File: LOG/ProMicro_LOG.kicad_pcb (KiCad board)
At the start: 2 copper layers, 17.8 x 30.5 mm, 16 parts, among them J1 Micro_SD_Card_Det, U1 DS3231MZ

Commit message: dump
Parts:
- A1: value Sparkfun_Pro_Micro_3V3 -> Sparkfun_Pro_Micro
- moved LOGO1 10.2 mm to (144.8, 80.0)
- renumbered JP2 to JP1, JP1 to JP2, JP4 to JP3, R6 to R1, R1 to R2, R2 to R3, R5 to R4, R3 to R5, R4 to R6
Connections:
- net Reset renamed ~RST
- A1 pad 10: (no net) -> INT
- A1 pad 11: INT -> (no net)
- A1 pad 3: (no net) -> GND
- A1 pad 7: TRG -> (no net)
- A1 pad 8: (no net) -> PWM
- JP1 pad 2: TRG -> PWM
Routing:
- net PWM: track 0.00 -> 18.7 mm, vias 0 -> 2
- net TRG: track 17.6 -> 0.00 mm, vias 2 -> 0
- net INT: track 12.0 -> 13.1 mm
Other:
- board text added: "3V3"
- board text added: "BTN"
- board text added: "CIPO"
- board text added: "COPI"
- board text added: "CS0"
- board text added: "CS1"
- board text added: "GND"
- board text added: "INT"
- board text added: "PWM"
- board text added: "RST"
- board text added: "SCK"
- board text added: "SCL"
- board text added: "SDA"
- board text added: "VBAT"
- board text added: "nerdyscout.github.io/ ProMicro/LOG v1.2"
- board text removed: "nerdyscout.github.io/ProMicro/LOG"
- board text removed: "v1.1"

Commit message: clean
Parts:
- moved R5 1.91 mm to (140.5, 95.9)
- moved R6 1.91 mm to (140.3, 97.8)
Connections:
- R5 pad 2: SDA -> SCL
- R6 pad 2: SCL -> SDA

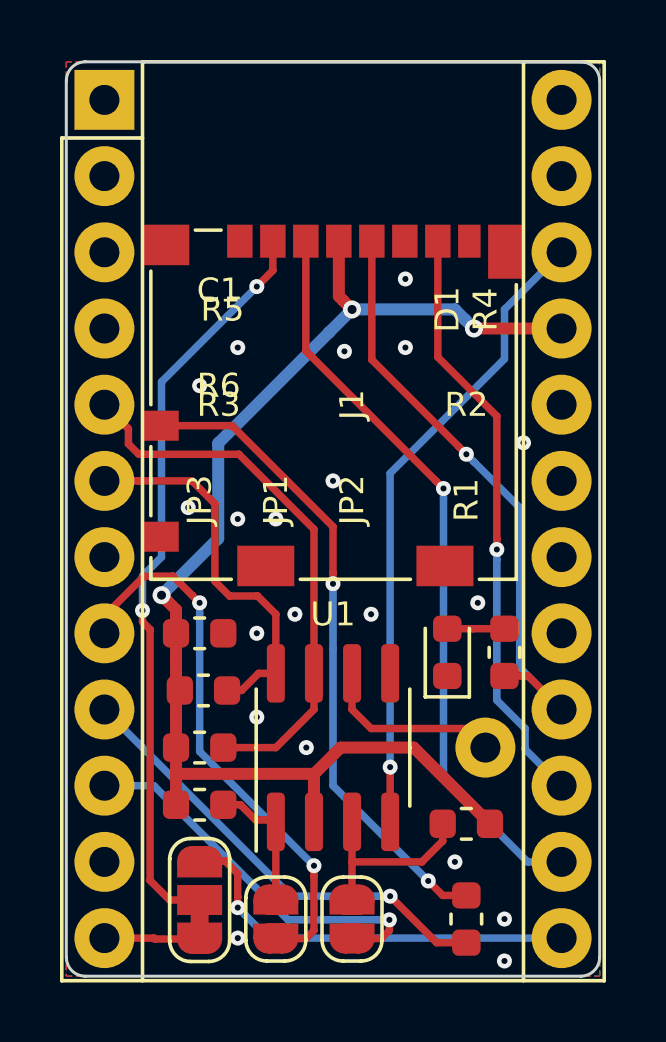
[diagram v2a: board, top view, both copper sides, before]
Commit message: make controller holes wide enough
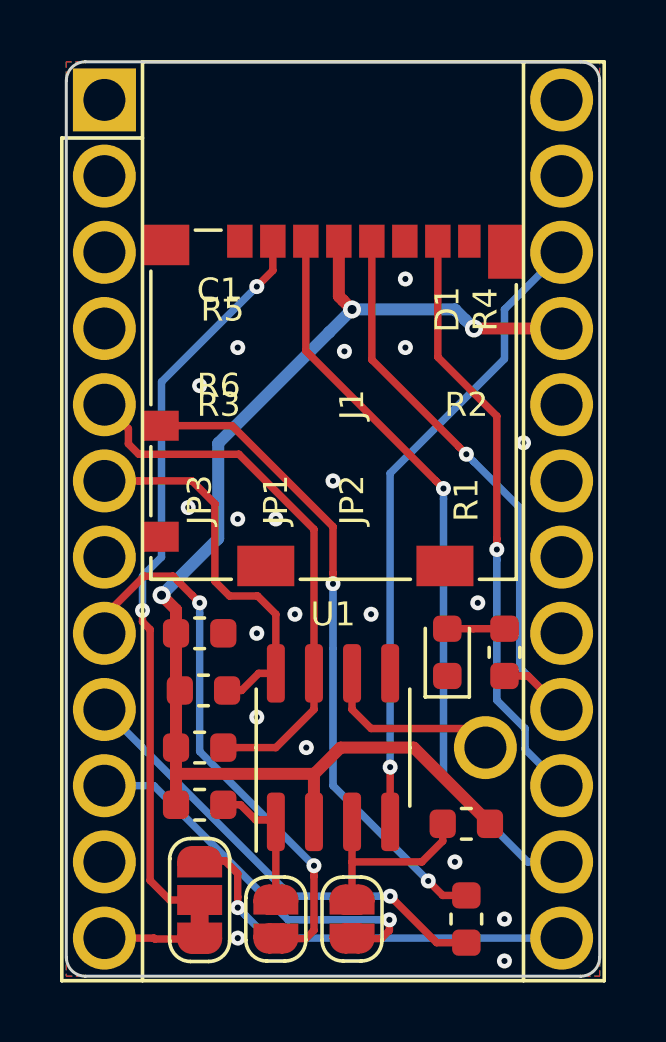
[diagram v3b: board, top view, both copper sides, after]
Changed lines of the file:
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@@
-(kicad_pcb (version 20171130) (host pcbnew 5.1.5+dfsg1-2build2)
+(kicad_pcb (version 20171130) (host pcbnew 5.1.5)
   (general
     (thickness 0.8)
@@
       (effects (font (size 1 1) (thickness 0.15)))
     )
-    (pad 1 thru_hole rect (at 0 0) (size 2 2) (drill 1) (layers *.Cu *.Mask))
-    (pad 2 thru_hole oval (at 0 2.54) (size 2 2) (drill 1) (layers *.Cu *.Mask))
-    (pad 3 thru_hole oval (at 0 5.08) (size 2 2) (drill 1) (layers *.Cu *.Mask)
+    (pad 1 thru_hole rect (at 0 0) (size 2.1 2.1) (drill 1.4) (layers *.Cu *.Mask))
+    (pad 2 thru_hole circle (at 0 2.54) (size 2.1 2.1) (drill 1.4) (layers *.Cu *.Mask))
+    (pad 3 thru_hole circle (at 0 5.08) (size 2.1 2.1) (drill 1.4) (layers *.Cu *.Mask)
       (net 1 GND))
-    (pad 13 thru_hole oval (at 15.24 27.94) (size 2 2) (drill 1) (layers *.Cu *.Mask)
+    (pad 13 thru_hole circle (at 15.24 27.94) (size 2.1 2.1) (drill 1.4) (layers *.Cu *.Mask)
       (net 8 CS0))
-    (pad 4 thru_hole oval (at 0 7.62) (size 2 2) (drill 1) (layers *.Cu *.Mask)
+    (pad 4 thru_hole circle (at 0 7.62) (size 2.1 2.1) (drill 1.4) (layers *.Cu *.Mask)
       (net 1 GND))
-    (pad 14 thru_hole oval (at 15.24 25.4) (size 2 2) (drill 1) (layers *.Cu *.Mask)
+    (pad 14 thru_hole circle (at 15.24 25.4) (size 2.1 2.1) (drill 1.4) (layers *.Cu *.Mask)
       (net 9 COPI))
-    (pad 5 thru_hole oval (at 0 10.16) (size 2 2) (drill 1) (layers *.Cu *.Mask)
+    (pad 5 thru_hole circle (at 0 10.16) (size 2.1 2.1) (drill 1.4) (layers *.Cu *.Mask)
       (net 10 SDA))
-    (pad 15 thru_hole oval (at 15.24 22.86) (size 2 2) (drill 1) (layers *.Cu *.Mask)
+    (pad 15 thru_hole circle (at 15.24 22.86) (size 2.1 2.1) (drill 1.4) (layers *.Cu *.Mask)
       (net 11 CIPO))
-    (pad 6 thru_hole oval (at 0 12.7) (size 2 2) (drill 1) (layers *.Cu *.Mask)
+    (pad 6 thru_hole circle (at 0 12.7) (size 2.1 2.1) (drill 1.4) (layers *.Cu *.Mask)
       (net 12 SCL))
-    (pad 16 thru_hole oval (at 15.24 20.32) (size 2 2) (drill 1) (layers *.Cu *.Mask)
+    (pad 16 thru_hole circle (at 15.24 20.32) (size 2.1 2.1) (drill 1.4) (layers *.Cu *.Mask)
       (net 13 SCK))
-    (pad 7 thru_hole oval (at 0 15.24) (size 2 2) (drill 1) (layers *.Cu *.Mask))
-    (pad 17 thru_hole oval (at 15.24 17.78) (size 2 2) (drill 1) (layers *.Cu *.Mask))
-    (pad 8 thru_hole oval (at 0 17.78) (size 2 2) (drill 1) (layers *.Cu *.Mask)
+    (pad 7 thru_hole circle (at 0 15.24) (size 2.1 2.1) (drill 1.4) (layers *.Cu *.Mask))
+    (pad 17 thru_hole circle (at 15.24 17.78) (size 2.1 2.1) (drill 1.4) (layers *.Cu *.Mask))
+    (pad 8 thru_hole circle (at 0 17.78) (size 2.1 2.1) (drill 1.4) (layers *.Cu *.Mask)
       (net 14 PWM))
-    (pad 18 thru_hole oval (at 15.24 15.24) (size 2 2) (drill 1) (layers *.Cu *.Mask))
-    (pad 9 thru_hole oval (at 0 20.32) (size 2 2) (drill 1) (layers *.Cu *.Mask)
+    (pad 18 thru_hole circle (at 15.24 15.24) (size 2.1 2.1) (drill 1.4) (layers *.Cu *.Mask))
+    (pad 9 thru_hole circle (at 0 20.32) (size 2.1 2.1) (drill 1.4) (layers *.Cu *.Mask)
       (net 15 BTN))
-    (pad 19 thru_hole oval (at 15.24 12.7) (size 2 2) (drill 1) (layers *.Cu *.Mask))
-    (pad 10 thru_hole oval (at 0 22.86) (size 2 2) (drill 1) (layers *.Cu *.Mask)
+    (pad 19 thru_hole circle (at 15.24 12.7) (size 2.1 2.1) (drill 1.4) (layers *.Cu *.Mask))
+    (pad 10 thru_hole circle (at 0 22.86) (size 2.1 2.1) (drill 1.4) (layers *.Cu *.Mask)
       (net 16 INT))
-    (pad 20 thru_hole oval (at 15.24 10.16) (size 2 2) (drill 1) (layers *.Cu *.Mask))
-    (pad 11 thru_hole oval (at 0 25.4) (size 2 2) (drill 1) (layers *.Cu *.Mask))
-    (pad 21 thru_hole oval (at 15.24 7.62) (size 2 2) (drill 1) (layers *.Cu *.Mask)
+    (pad 20 thru_hole circle (at 15.24 10.16) (size 2.1 2.1) (drill 1.4) (layers *.Cu *.Mask))
+    (pad 11 thru_hole circle (at 0 25.4) (size 2.1 2.1) (drill 1.4) (layers *.Cu *.Mask))
+    (pad 21 thru_hole circle (at 15.24 7.62) (size 2.1 2.1) (drill 1.4) (layers *.Cu *.Mask)
       (net 2 +3V3))
-    (pad 12 thru_hole oval (at 0 27.94) (size 2 2) (drill 1) (layers *.Cu *.Mask)
+    (pad 12 thru_hole circle (at 0 27.94) (size 2.1 2.1) (drill 1.4) (layers *.Cu *.Mask)
       (net 17 CS1))
-    (pad 22 thru_hole oval (at 15.24 5.08) (size 2 2) (drill 1) (layers *.Cu *.Mask)
+    (pad 22 thru_hole circle (at 15.24 5.08) (size 2.1 2.1) (drill 1.4) (layers *.Cu *.Mask)
       (net 18 ~RST))
-    (pad 23 thru_hole oval (at 15.24 2.54) (size 2 2) (drill 1) (layers *.Cu *.Mask)
+    (pad 23 thru_hole circle (at 15.24 2.54) (size 2.1 2.1) (drill 1.4) (layers *.Cu *.Mask)
       (net 1 GND))
-    (pad 24 thru_hole oval (at 15.24 0) (size 2 2) (drill 1) (layers *.Cu *.Mask))
+    (pad 24 thru_hole circle (at 15.24 0) (size 2.1 2.1) (drill 1.4) (layers *.Cu *.Mask))
     (model ${KISYS3DMOD}/Module.3dshapes/Sparkfun_Pro_Micro.wrl
       (at (xyz 0 0 0))
@@
       (effects (font (size 0.8 0.8) (thickness 0.2)) (justify mirror))
     )
-    (pad 1 thru_hole circle (at 0 0) (size 2 2) (drill 1) (layers *.Cu *.Mask)
+    (pad 1 thru_hole circle (at 0 0) (size 2.1 2.1) (drill 1.4) (layers *.Cu *.Mask)
       (net 3 "Net-(TP1-Pad1)"))
   )

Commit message: update PCBs to be stackable
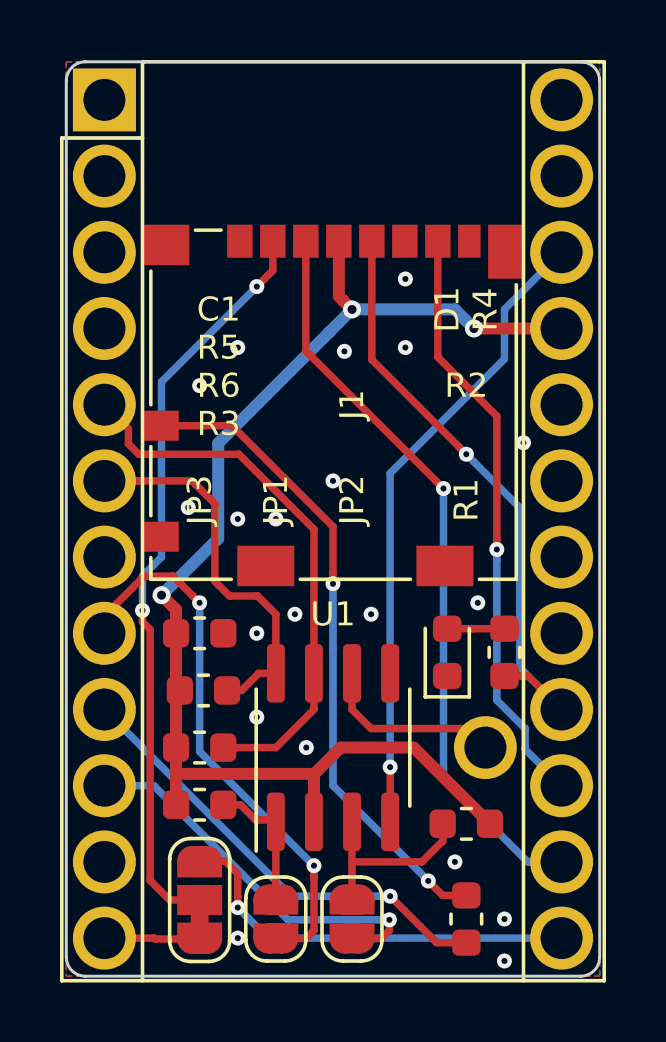
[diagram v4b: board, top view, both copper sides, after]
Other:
- board text added: "nerdyscout.github.io/ ProMicro/LOG v1.3"
- board text removed: "nerdyscout.github.io/ ProMicro/LOG v1.2"
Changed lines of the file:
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@@
   (title_block
     (title ProMicro_LOG)
-    (date 2020-10-12)
-    (rev v1.2)
+    (date 2020-11-21)
+    (rev v1.3)
   )
   (layers
     (0 F.Cu mixed)
     (31 B.Cu mixed)
-    (32 B.Adhes user hide)
-    (33 F.Adhes user hide)
-    (34 B.Paste user hide)
+    (32 B.Adhes user)
+    (33 F.Adhes user)
+    (34 B.Paste user)
     (35 F.Paste user)
-    (36 B.SilkS user hide)
+    (36 B.SilkS user)
     (37 F.SilkS user)
-    (38 B.Mask user hide)
+    (38 B.Mask user)
     (39 F.Mask user)
-    (40 Dwgs.User user hide)
-    (41 Cmts.User user hide)
-    (42 Eco1.User user hide)
-    (43 Eco2.User user hide)
+    (40 Dwgs.User user)
+    (41 Cmts.User user)
+    (42 Eco1.User user)
+    (43 Eco2.User user)
     (44 Edge.Cuts user)
-    (45 Margin user hide)
-    (46 B.CrtYd user hide)
+    (45 Margin user)
+    (46 B.CrtYd user)
     (47 F.CrtYd user)
     (48 B.Fab user hide)
-    (49 F.Fab user)
+    (49 F.Fab user hide)
   )
   (setup
@@
     (tags capacitor)
     (attr smd)
-    (fp_text reference C1 (at 0.635 -11.43 180) (layer F.SilkS)
+    (fp_text reference C1 (at 0.635 -10.795 180) (layer F.SilkS)
       (effects (font (size 0.8 0.8) (thickness 0.2)))
     )
@@
     (tags resistor)
     (attr smd)
-    (fp_text reference R5 (at 0.635 -12.7) (layer F.SilkS)
+    (fp_text reference R5 (at 0.508 -11.43) (layer F.SilkS)
       (effects (font (size 0.8 0.8) (thickness 0.2)))
     )
@@
     (tags resistor)
     (attr smd)
-    (fp_text reference R3 (at 0.635 -13.335) (layer F.SilkS)
+    (fp_text reference R3 (at 0.635 -12.7) (layer F.SilkS)
       (effects (font (size 0.8 0.8) (thickness 0.2)))
     )
@@
     (tags resistor)
     (attr smd)
-    (fp_text reference R2 (at 0 13.97) (layer F.SilkS)
+    (fp_text reference R2 (at 0 14.605) (layer F.SilkS)
       (effects (font (size 0.8 0.8) (thickness 0.2)))
     )
@@
     (effects (font (size 0.8 0.8) (thickness 0.2)) (justify mirror))
   )
-  (gr_text "nerdyscout.github.io/\nProMicro/LOG\nv1.2" (at 144.78 84.455 90) (layer B.SilkS)
+  (gr_text "nerdyscout.github.io/\nProMicro/LOG\nv1.3" (at 144.78 84.455 90) (layer B.SilkS)
     (effects (font (size 1 1) (thickness 0.25)) (justify left mirror))
   )

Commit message: update PCBS
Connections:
- A1 pad 1: (no net) -> Net-(A1-Pad1)
- A1 pad 11: (no net) -> Net-(A1-Pad11)
- A1 pad 17: (no net) -> Net-(A1-Pad17)
- A1 pad 18: (no net) -> Net-(A1-Pad18)
- A1 pad 19: (no net) -> Net-(A1-Pad19)
- A1 pad 2: (no net) -> Net-(A1-Pad2)
- A1 pad 20: (no net) -> Net-(A1-Pad20)
- A1 pad 24: (no net) -> Net-(A1-Pad24)
- A1 pad 7: (no net) -> Net-(A1-Pad7)
- J1 pad 1: (no net) -> Net-(J1-Pad1)
- J1 pad 8: (no net) -> Net-(J1-Pad8)
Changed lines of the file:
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@@
     (zones 0)
     (modules 16)
-    (nets 20)
+    (nets 31)
   )
   (page A4)
@@
   (net 18 ~RST)
   (net 19 CS)
+  (net 20 "Net-(A1-Pad1)")
+  (net 21 "Net-(A1-Pad2)")
+  (net 22 "Net-(A1-Pad7)")
+  (net 23 "Net-(A1-Pad17)")
+  (net 24 "Net-(A1-Pad18)")
+  (net 25 "Net-(A1-Pad19)")
+  (net 26 "Net-(A1-Pad20)")
+  (net 27 "Net-(A1-Pad11)")
+  (net 28 "Net-(A1-Pad24)")
+  (net 29 "Net-(J1-Pad8)")
+  (net 30 "Net-(J1-Pad1)")
   (net_class Default "This is the default net class."
     (clearance 0.2)
@@
     (add_net CS1)
     (add_net INT)
+    (add_net "Net-(A1-Pad1)")
+    (add_net "Net-(A1-Pad11)")
+    (add_net "Net-(A1-Pad17)")
+    (add_net "Net-(A1-Pad18)")
+    (add_net "Net-(A1-Pad19)")
+    (add_net "Net-(A1-Pad2)")
+    (add_net "Net-(A1-Pad20)")
+    (add_net "Net-(A1-Pad24)")
+    (add_net "Net-(A1-Pad7)")
     (add_net "Net-(D1-Pad2)")
+    (add_net "Net-(J1-Pad1)")
+    (add_net "Net-(J1-Pad8)")
     (add_net "Net-(J1-Pad9)")
     (add_net "Net-(JP1-Pad1)")
@@
       (effects (font (size 1 1) (thickness 0.15)))
     )
-    (pad 1 thru_hole rect (at 0 0) (size 2.1 2.1) (drill 1.4) (layers *.Cu *.Mask))
-    (pad 2 thru_hole circle (at 0 2.54) (size 2.1 2.1) (drill 1.4) (layers *.Cu *.Mask))
+    (pad 1 thru_hole rect (at 0 0) (size 2.1 2.1) (drill 1.4) (layers *.Cu *.Mask)
+      (net 20 "Net-(A1-Pad1)"))
+    (pad 2 thru_hole circle (at 0 2.54) (size 2.1 2.1) (drill 1.4) (layers *.Cu *.Mask)
+      (net 21 "Net-(A1-Pad2)"))
     (pad 3 thru_hole circle (at 0 5.08) (size 2.1 2.1) (drill 1.4) (layers *.Cu *.Mask)
       (net 1 GND))
@@
     (pad 16 thru_hole circle (at 15.24 20.32) (size 2.1 2.1) (drill 1.4) (layers *.Cu *.Mask)
       (net 13 SCK))
-    (pad 7 thru_hole circle (at 0 15.24) (size 2.1 2.1) (drill 1.4) (layers *.Cu *.Mask))
-    (pad 17 thru_hole circle (at 15.24 17.78) (size 2.1 2.1) (drill 1.4) (layers *.Cu *.Mask))
+    (pad 7 thru_hole circle (at 0 15.24) (size 2.1 2.1) (drill 1.4) (layers *.Cu *.Mask)
+      (net 22 "Net-(A1-Pad7)"))
+    (pad 17 thru_hole circle (at 15.24 17.78) (size 2.1 2.1) (drill 1.4) (layers *.Cu *.Mask)
+      (net 23 "Net-(A1-Pad17)"))
     (pad 8 thru_hole circle (at 0 17.78) (size 2.1 2.1) (drill 1.4) (layers *.Cu *.Mask)
       (net 14 PWM))
-    (pad 18 thru_hole circle (at 15.24 15.24) (size 2.1 2.1) (drill 1.4) (layers *.Cu *.Mask))
+    (pad 18 thru_hole circle (at 15.24 15.24) (size 2.1 2.1) (drill 1.4) (layers *.Cu *.Mask)
+      (net 24 "Net-(A1-Pad18)"))
     (pad 9 thru_hole circle (at 0 20.32) (size 2.1 2.1) (drill 1.4) (layers *.Cu *.Mask)
       (net 15 BTN))
-    (pad 19 thru_hole circle (at 15.24 12.7) (size 2.1 2.1) (drill 1.4) (layers *.Cu *.Mask))
+    (pad 19 thru_hole circle (at 15.24 12.7) (size 2.1 2.1) (drill 1.4) (layers *.Cu *.Mask)
+      (net 25 "Net-(A1-Pad19)"))
     (pad 10 thru_hole circle (at 0 22.86) (size 2.1 2.1) (drill 1.4) (layers *.Cu *.Mask)
       (net 16 INT))
-    (pad 20 thru_hole circle (at 15.24 10.16) (size 2.1 2.1) (drill 1.4) (layers *.Cu *.Mask))
-    (pad 11 thru_hole circle (at 0 25.4) (size 2.1 2.1) (drill 1.4) (layers *.Cu *.Mask))
+    (pad 20 thru_hole circle (at 15.24 10.16) (size 2.1 2.1) (drill 1.4) (layers *.Cu *.Mask)
+      (net 26 "Net-(A1-Pad20)"))
+    (pad 11 thru_hole circle (at 0 25.4) (size 2.1 2.1) (drill 1.4) (layers *.Cu *.Mask)
+      (net 27 "Net-(A1-Pad11)"))
     (pad 21 thru_hole circle (at 15.24 7.62) (size 2.1 2.1) (drill 1.4) (layers *.Cu *.Mask)
       (net 2 +3V3))
@@
     (pad 23 thru_hole circle (at 15.24 2.54) (size 2.1 2.1) (drill 1.4) (layers *.Cu *.Mask)
       (net 1 GND))
-    (pad 24 thru_hole circle (at 15.24 0) (size 2.1 2.1) (drill 1.4) (layers *.Cu *.Mask))
+    (pad 24 thru_hole circle (at 15.24 0) (size 2.1 2.1) (drill 1.4) (layers *.Cu *.Mask)
+      (net 28 "Net-(A1-Pad24)"))
     (model ${KISYS3DMOD}/Module.3dshapes/Sparkfun_Pro_Micro.wrl
       (at (xyz 0 0 0))
@@
     (pad 2 smd rect (at -2.005 -5.45) (size 0.85 1.1) (layers F.Cu F.Paste F.Mask)
       (net 19 CS))
-    (pad 8 smd rect (at 4.545 -5.45) (size 0.75 1.1) (layers F.Cu F.Paste F.Mask))
-    (pad 1 smd rect (at -3.105 -5.45) (size 0.85 1.1) (layers F.Cu F.Paste F.Mask))
+    (pad 8 smd rect (at 4.545 -5.45) (size 0.75 1.1) (layers F.Cu F.Paste F.Mask)
+      (net 29 "Net-(J1-Pad8)"))
+    (pad 1 smd rect (at -3.105 -5.45) (size 0.85 1.1) (layers F.Cu F.Paste F.Mask)
+      (net 30 "Net-(J1-Pad1)"))
     (model ${KISYS3DMOD}/Connector_Card.3dshapes/microSD_HC_Molex_104031-0811.wrl
       (at (xyz 0 0 0))
@@
   (segment (start 137.16 93.400001) (end 138.485001 92.075) (width 0.25) (layer F.Cu) (net 14))
   (segment (start 137.16 93.98) (end 137.16 93.400001) (width 0.25) (layer F.Cu) (net 14))
-  (segment (start 146.331447 102.743) (end 146.685 102.743) (width 0.25) (layer B.Cu) (net 15))
-  (segment (start 137.16 96.52) (end 143.383 102.743) (width 0.25) (layer B.Cu) (net 15))
-  (segment (start 143.383 102.743) (end 146.331447 102.743) (width 0.25) (layer B.Cu) (net 15))
   (via (at 146.685 102.743) (size 0.5) (drill 0.2) (layers F.Cu B.Cu) (net 15))
   (segment (start 149.225 104.2925) (end 148.2345 104.2925) (width 0.25) (layer F.Cu) (net 15))
   (segment (start 148.2345 104.2925) (end 146.685 102.743) (width 0.25) (layer F.Cu) (net 15))
+  (segment (start 146.331447 102.743) (end 146.685 102.743) (width 0.25) (layer B.Cu) (net 15))
+  (segment (start 143.383 102.743) (end 146.331447 102.743) (width 0.25) (layer B.Cu) (net 15))
+  (segment (start 137.16 96.52) (end 143.383 102.743) (width 0.25) (layer B.Cu) (net 15))
   (via (at 146.659408 103.530596) (size 0.5) (drill 0.2) (layers F.Cu B.Cu) (net 16))
   (segment (start 145.415 104.155) (end 146.388557 104.155) (width 0.25) (layer F.Cu) (net 16))
@@
   (segment (start 146.659408 103.884149) (end 146.659408 103.530596) (width 0.25) (layer F.Cu) (net 16))
   (segment (start 137.795 99.06) (end 137.16 99.06) (width 0.25) (layer B.Cu) (net 16))
-  (segment (start 143.281596 103.530596) (end 138.811 99.06) (width 0.25) (layer B.Cu) (net 16))
-  (segment (start 138.811 99.06) (end 137.795 99.06) (width 0.25) (layer B.Cu) (net 16))
-  (segment (start 146.659408 103.530596) (end 143.281596 103.530596) (width 0.25) (layer B.Cu) (net 16))
+  (segment (start 138.684 99.06) (end 137.795 99.06) (width 0.25) (layer B.Cu) (net 16))
+  (segment (start 143.154596 103.530596) (end 138.684 99.06) (width 0.25) (layer B.Cu) (net 16))
+  (segment (start 146.659408 103.530596) (end 143.154596 103.530596) (width 0.25) (layer B.Cu) (net 16))
   (segment (start 140.335 104.17) (end 138.841 104.17) (width 0.25) (layer F.Cu) (net 17))
   (segment (start 138.811 104.14) (end 137.16 104.14) (width 0.25) (layer F.Cu) (net 17))
@@
   (segment (start 146.685 100.265) (end 146.685 98.44001) (width 0.25) (layer F.Cu) (net 18))
   (via (at 146.685 98.44001) (size 0.5) (drill 0.2) (layers F.Cu B.Cu) (net 18))
-  (segment (start 150.495 84.836) (end 146.685 88.646) (width 0.25) (layer B.Cu) (net 18))
   (segment (start 146.685 88.646) (end 146.685 98.44001) (width 0.25) (layer B.Cu) (net 18))
-  (segment (start 150.495 83.185) (end 150.495 84.836) (width 0.25) (layer B.Cu) (net 18))
-  (segment (start 152.4 81.28) (end 150.495 83.185) (width 0.25) (layer B.Cu) (net 18))
+  (segment (start 150.876 84.455) (end 146.685 88.646) (width 0.25) (layer B.Cu) (net 18))
+  (segment (start 150.876 82.804) (end 150.876 84.455) (width 0.25) (layer B.Cu) (net 18))
+  (segment (start 152.4 81.28) (end 150.876 82.804) (width 0.25) (layer B.Cu) (net 18))
   (via (at 142.24 82.423) (size 0.5) (drill 0.2) (layers F.Cu B.Cu) (net 19))
   (segment (start 142.775 81.888) (end 142.24 82.423) (width 0.25) (layer F.Cu) (net 19))
   (segment (start 142.775 80.91) (end 142.775 81.888) (width 0.25) (layer F.Cu) (net 19))
   (via (at 138.43 93.218) (size 0.5) (drill 0.2) (layers F.Cu B.Cu) (net 19))
-  (segment (start 139.065 91.44) (end 138.43 92.075) (width 0.25) (layer B.Cu) (net 19))
-  (segment (start 139.065 85.598) (end 139.065 91.44) (width 0.25) (layer B.Cu) (net 19))
-  (segment (start 138.43 92.075) (end 138.43 93.218) (width 0.25) (layer B.Cu) (net 19))
-  (segment (start 142.24 82.423) (end 139.065 85.598) (width 0.25) (layer B.Cu) (net 19))
   (segment (start 138.43 93.599) (end 138.43 93.218) (width 0.25) (layer F.Cu) (net 19))
   (segment (start 138.684 93.853) (end 138.43 93.599) (width 0.25) (layer F.Cu) (net 19))
@@
   (segment (start 139.335 102.87) (end 138.684 102.219) (width 0.25) (layer F.Cu) (net 19))
   (segment (start 140.335 102.87) (end 139.335 102.87) (width 0.25) (layer F.Cu) (net 19))
+  (segment (start 142.24 82.423) (end 139.065 85.598) (width 0.25) (layer B.Cu) (net 19))
+  (segment (start 139.065 85.598) (end 139.065 91.44) (width 0.25) (layer B.Cu) (net 19))
+  (segment (start 139.065 91.44) (end 138.43 92.075) (width 0.25) (layer B.Cu) (net 19))
+  (segment (start 138.43 92.075) (end 138.43 93.218) (width 0.25) (layer B.Cu) (net 19))
   (zone (net 1) (net_name GND) (layer B.Cu) (hatch edge 0.508)
     (connect_pads (clearance 0.125))

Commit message: update design
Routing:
- net CS: track 25.1 -> 35.9 mm
- net CIPO: track 19.9 -> 24.2 mm
- net BTN: track 15.3 -> 17.9 mm
- net COPI: track 24.9 -> 25.6 mm
- net CS0: track 13.8 -> 14.4 mm
- net PWM: track 18.6 -> 18.0 mm
- net GND: vias 20 -> 16
